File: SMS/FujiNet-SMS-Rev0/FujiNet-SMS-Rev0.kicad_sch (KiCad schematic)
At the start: 0 parts

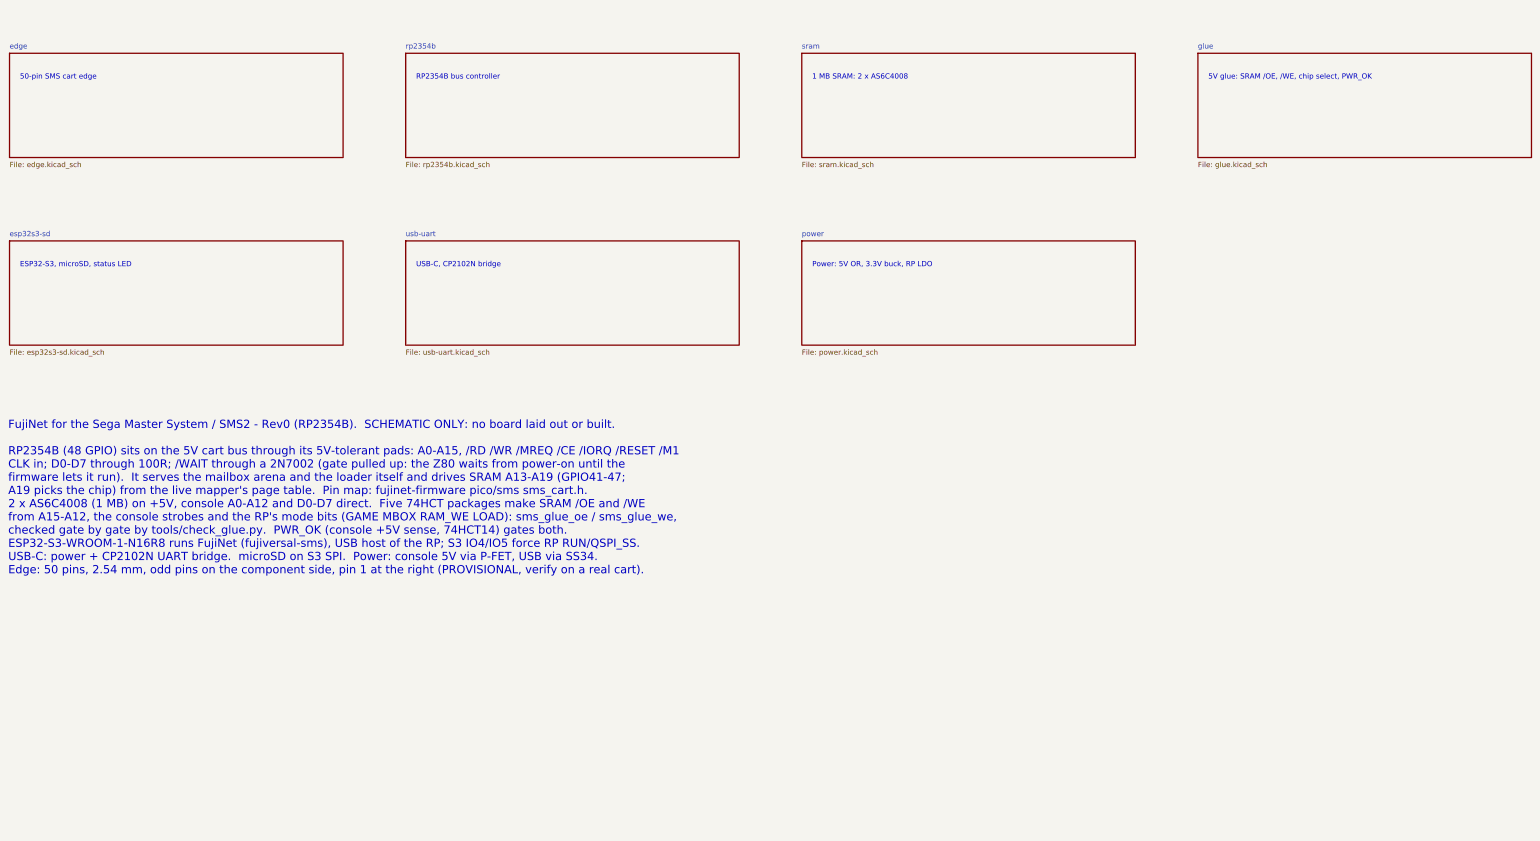
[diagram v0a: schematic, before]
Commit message: SMS Rev0: audit with kicad-happy + datasheets, fix the edge, redraw the schematic
Edge connector: every source (SMS Power slot diagram, little-scale, a 171-5519
scan, raphnet, the barbeque and reidrac footprints) puts the EVEN pins on the
component / label side with pins 1/2 at the right.  The schematic-only
footprint had the faces swapped, which would have put console +5V on /WR.
make_edge_fp.py now writes even pads on F.Cu, odd on B.Cu, 1.75 x 8.75 mm
fingers 0.75-9.5 mm from the edge on a 65.8 mm tab; check_nets.py asserts it
and tools/audit/edge_orientation.py checks it against the sources.

kicad-happy + datasheet audit (docs/design-review-rev0.md Part 1, 27 deep
review findings, gate 27/27): R_VBPD 4.7k VBUS pull-down (SS34 leakage lifts
the P-FET gate), /WAIT gate pull-up 10k -> 4.7k (GPIO34's reset pull-down vs
the 2N7002's 2.5 V threshold), 10 uF bulk on the console 5V.

Schematic: hierarchical sheets wired on a root block diagram (edge -> RP2354B
-> ESP32-S3 -> USB, glue and SRAM under the RP, power below); every sheet
drawn left to right, the glue as a wired logic network by gate depth, the
RP2354B mirrored so its bus faces the console, small sheets on A4.  Parts
are addressed by key (design.py), no more NES reference aliasing.  sch_draw
gains hierarchical labels, sheet blocks, a bus graph and flag / power-pin
lints; gen_sch checks the hierarchy against design.py and names nets by
their last path element (one bus vector per bus: KiCad joins differing
vectors by position).  ERC 0, check_nets 437/437, check_glue 8192/8192.

JLC CPL rotations measured against the EasyEDA footprint of every LCSC part
(tools/audit/jlc); the AS6C4008 has no EasyEDA footprint.

Co-Authored-By: Claude Opus 5.5 <noreply@anthropic.com>
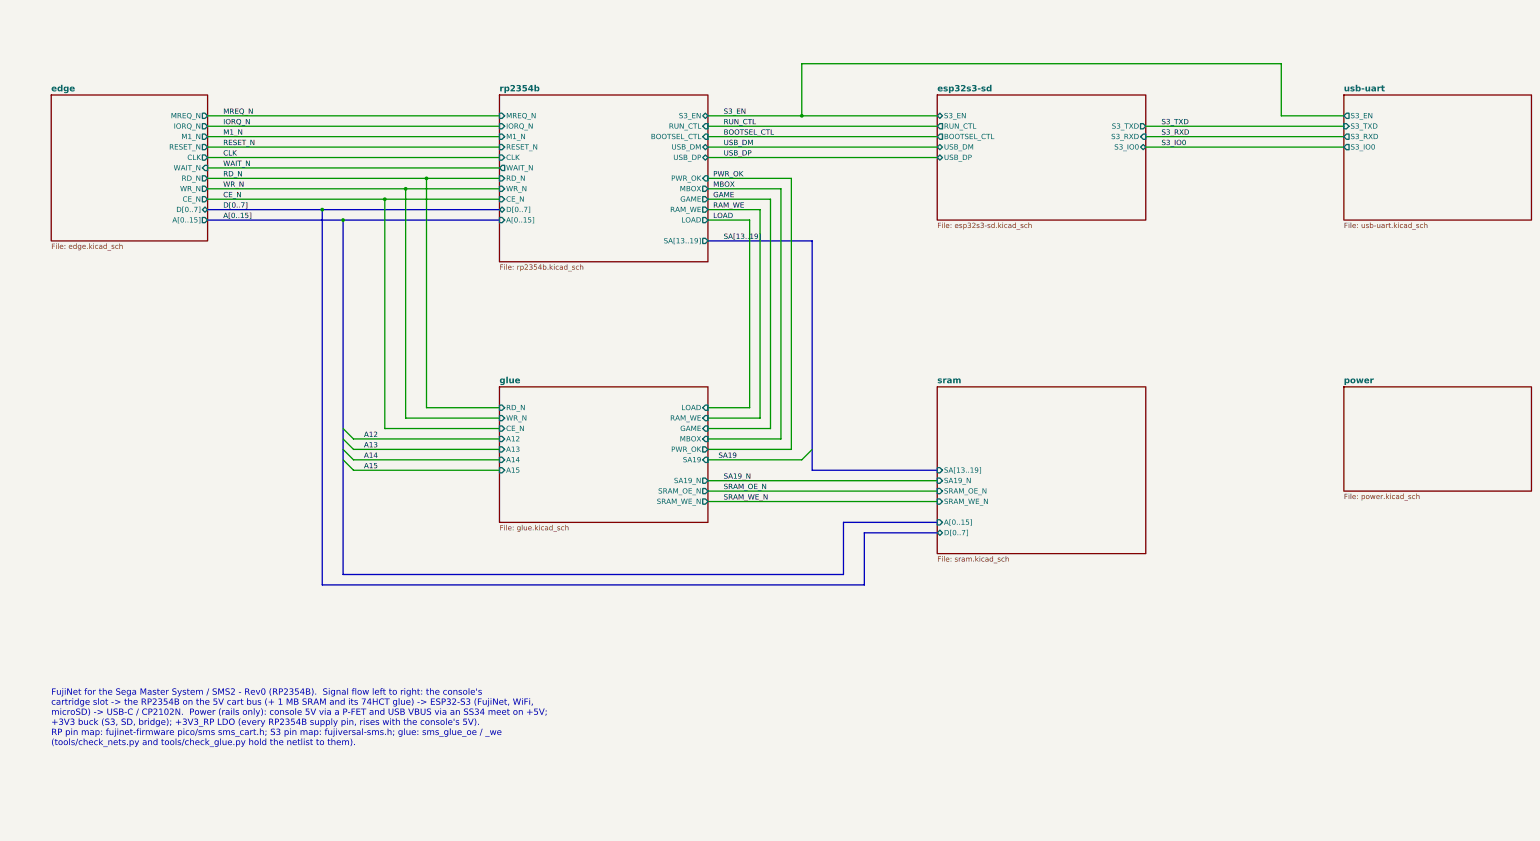
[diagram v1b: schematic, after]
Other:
- sheet edge ports: added A[0..15], CE_N, CLK, D[0..7], IORQ_N, M1_N, MREQ_N, RD_N, RESET_N, WAIT_N, WR_N; removed none
- sheet esp32s3-sd ports: added BOOTSEL_CTL, RUN_CTL, S3_EN, S3_IO0, S3_RXD, S3_TXD, USB_DM, USB_DP; removed none
- sheet glue ports: added A12, A13, A14, A15, CE_N, GAME, LOAD, MBOX, PWR_OK, RAM_WE, RD_N, SA19, SA19_N, SRAM_OE_N, SRAM_WE_N, WR_N; removed none
- sheet rp2354b ports: added A[0..15], BOOTSEL_CTL, CE_N, CLK, D[0..7], GAME, IORQ_N, LOAD, M1_N, MBOX, MREQ_N, PWR_OK, RAM_WE, RD_N, RESET_N, RUN_CTL, S3_EN, SA[13..19], USB_DM, USB_DP, WAIT_N, WR_N; removed none
- sheet sram ports: added A[0..15], D[0..7], SA19_N, SA[13..19], SRAM_OE_N, SRAM_WE_N; removed none
- sheet usb-uart ports: added S3_EN, S3_IO0, S3_RXD, S3_TXD; removed none
- note added: "FujiNet for the Sega Master System / SMS2 - Rev0 (RP2354B). Signal flow left to right: the console's cartridge slot -> the RP2354B on the 5V cart bus (+ 1 MB SRAM and its 74HCT glue) -> ESP32-S3 (FujiNet, WiFi, microSD) -> USB-C / CP2102N. Power (rails only): console 5V via a P-FET and USB VBUS via an SS34 meet on +5V; +3V3 buck (S3, SD, bridge); +3V3_RP LDO (every RP2354B supply pin, rises with 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"
- note removed: "1 MB SRAM: 2 x AS6C4008"
- note removed: "50-pin SMS cart edge"
- note removed: "5V glue: SRAM /OE, /WE, chip select, PWR_OK"
- note removed: "ESP32-S3, microSD, status LED"
- note removed: "FujiNet for the Sega Master System / SMS2 - Rev0 (RP2354B). SCHEMATIC ONLY: no board laid out or built. RP2354B (48 GPIO) sits on the 5V cart bus through its 5V-tolerant pads: A0-A15, /RD /WR /MREQ /CE /IORQ /RESET /M1 CLK in; D0-D7 through 100R; /WAIT through a 2N7002 (gate pulled up: the Z80 waits from power-on until the firmware lets it run). It serves the mailbox arena and the loader itself a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"
- note removed: "Power: 5V OR, 3.3V buck, RP LDO"
- note removed: "RP2354B bus controller"
- note removed: "USB-C, CP2102N bridge"

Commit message: SMS Rev0 v2: co-designed floorplan, region sheets, E9 pull-downs, frozen refs and nets
Floorplan study (docs/floorplan-study.md): the SMS edge is the JEDEC
32-pin memory pinout unrolled, so SRAM0 standing upright in the ROM spot
takes A0-A12 / D0-D7 / GND with no crossing.  gen_pcb.sram0_fanin draws
that fan-in locked (funnel, two corner wraps, B-finger jog vias, escape
vias for CE# and OE#).  Four candidates scored and trial-routed in
parallel; P3 (RP2354B straight north of SRAM0, SRAM1 west, glue east over
the strobes) routes best (45 unrouted after 4 passes vs 50 for the first
layout) and reads straight across on the schematic page.

- placement.py: candidates as blocks; the RP2354B + ring as a rigid macro
  (turns as a whole, dvdd_island turns with it); per-variant In4 +5V
  island polygon; label area for the shell
- design.py: sheets are board regions (cart-bus, rp-core, fujinet, usb,
  power); the RP2354B as a two-unit symbol (GPIO on cart-bus, core on
  rp-core); resistor packs one unit per resistor; RP2350-E9 4.7k
  pull-downs on GAME/LOAD/RAM_WE/MBOX/SA19 (check_nets asserts <= 8.2k);
  bring-up pads (CE, OE, WE, PWR_OK, rails, DVDD)
- geographic references (tools/annotate.py -> tools/refs.lock); net names
  frozen in tools/nets.lock (gen_sch fails if a redraw changes one)
- sch_draft.py: an every-pin-labelled draft of the final hierarchy so the
  board is built while the sheets are drawn; sch_draw lint for wired
  sheets (one piece per net, no 4-way junctions, wires clear of text,
  crossing count); sch_place.py mirror check
- check_parts_inside: footprint keep-outs (the S3 antenna bars parts)
- shell: RESET plunger redesigned (captive flange under the guide, stem
  on the TS-1187A actuator, travel asserts, interference part)

ERC 0, parity 126/126, check_nets 442/442, check_glue 8192/8192.
Board placed, not routed yet.

Co-Authored-By: Claude Opus 5.5 <noreply@anthropic.com>
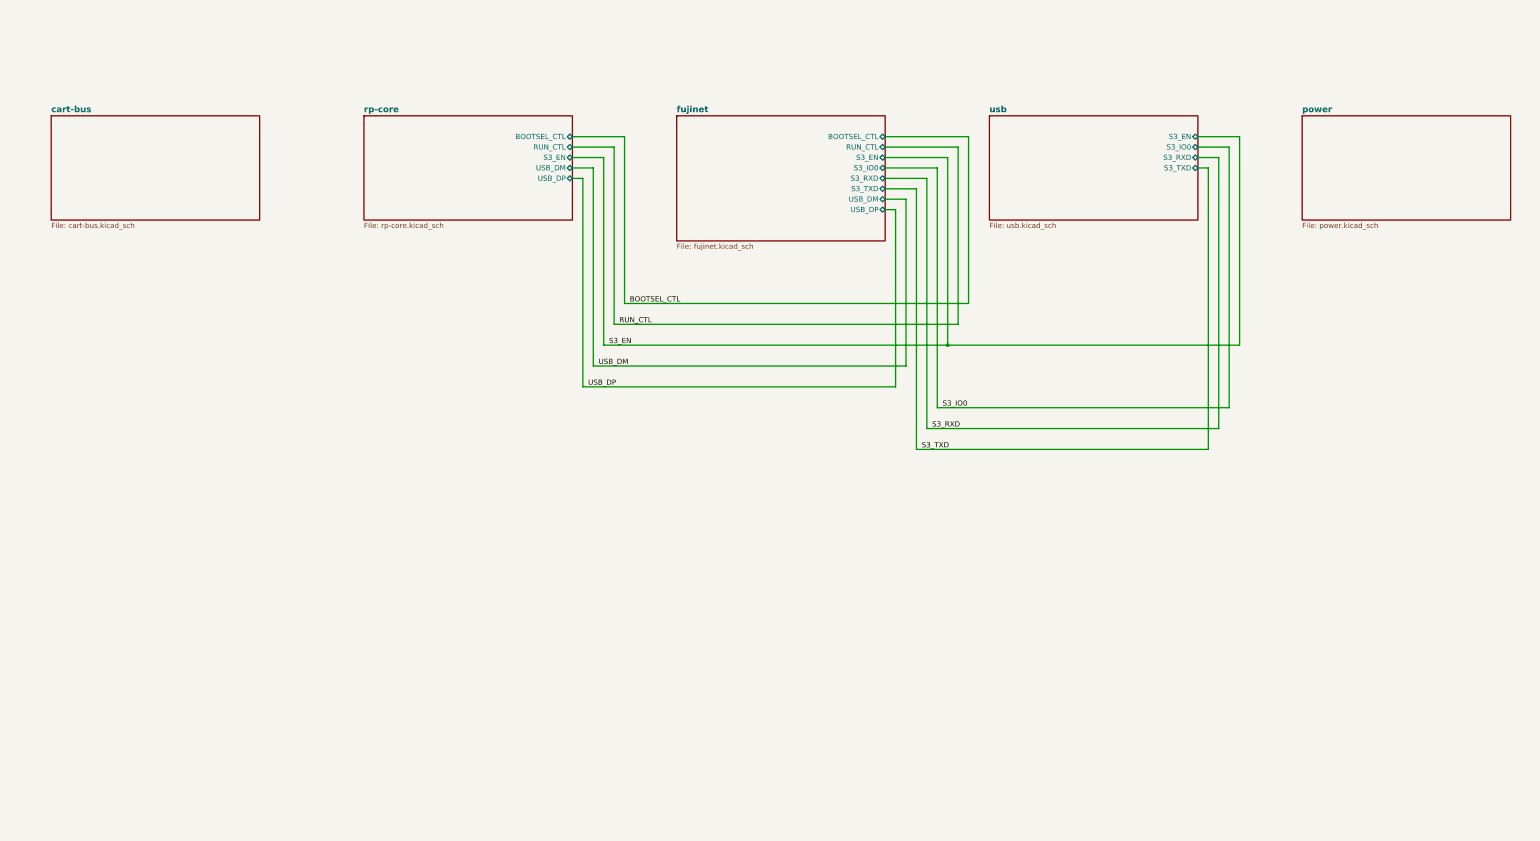
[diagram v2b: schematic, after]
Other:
- removed sheet edge
- removed sheet esp32s3-sd
- removed sheet glue
- removed sheet rp2354b
- removed sheet sram
- removed sheet usb-uart
- added sheet cart-bus (cart-bus.kicad_sch)
- added sheet fujinet (fujinet.kicad_sch)
- added sheet rp-core (rp-core.kicad_sch)
- added sheet usb (usb.kicad_sch)
- note removed: "FujiNet for the Sega Master System / SMS2 - Rev0 (RP2354B). Signal flow left to right: the console's cartridge slot -> the RP2354B on the 5V cart bus (+ 1 MB SRAM and its 74HCT glue) -> ESP32-S3 (FujiNet, WiFi, microSD) -> USB-C / CP2102N. Power (rails only): console 5V via a P-FET and USB VBUS via an SS34 meet on +5V; +3V3 buck (S3, SD, bridge); +3V3_RP LDO (every RP2354B supply pin, rises with 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"

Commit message: SMS Rev0 v2: redraw every sheet to mirror the board
Each sheet is now hand-placed in tools/sch_layout.py from where its parts
sit on the board, turned so the edge fingers face left (south -> left,
north -> right, west -> top, east -> bottom), and every connection on a
sheet is a wire:

- rp-core: the RP2354B core unit with its decoupling ring at the pins, the
  regulator corner, the crystal, SWD, RUN / BOOTSEL and the RESET diode
  (planar).
- fujinet: a functional ESP32-S3 symbol, EN / BOOT, the WS2812, and the
  microSD's SPI lines stepping into the socket with the pull-ups between
  them (planar).
- usb: a functional USB-C symbol, the CP2102N mirrored to face the
  receptacle, and the auto-program pair.  This page has one crossing, which
  cannot be avoided: RTS and DTR sit side by side on the bridge and each
  feeds the base of one transistor and the emitter of the other.
- power: the CONS_5V / VBUS OR on one +5V line, the LDO above it, the buck
  below it, and the rail PWR_FLAGs grouped together (planar).
- root: the board outline at 2:1, turned the same way, with each sheet's
  block at its region and the nine signals between sheets wired without a
  crossing; notes cover the stack-up and the firmware contract.

Gates: gen_sch.py checks the mirror (Kendall tau >= 0.85 per axis for the
major parts, multi-unit packages counted at the centre of their units,
parts within 5 mm on the board counted as level; every sheet is at
1.00 / 1.00) and a crossing budget per sheet (cart-bus 75, usb 1,
others 0).  ERC is 0 at all severities, netlist parity holds, the net
names equal tools/nets.lock, check_nets passes 442/442, check_glue
8192/8192, and edge_orientation passes.

Co-Authored-By: Claude Opus 5.5 <noreply@anthropic.com>
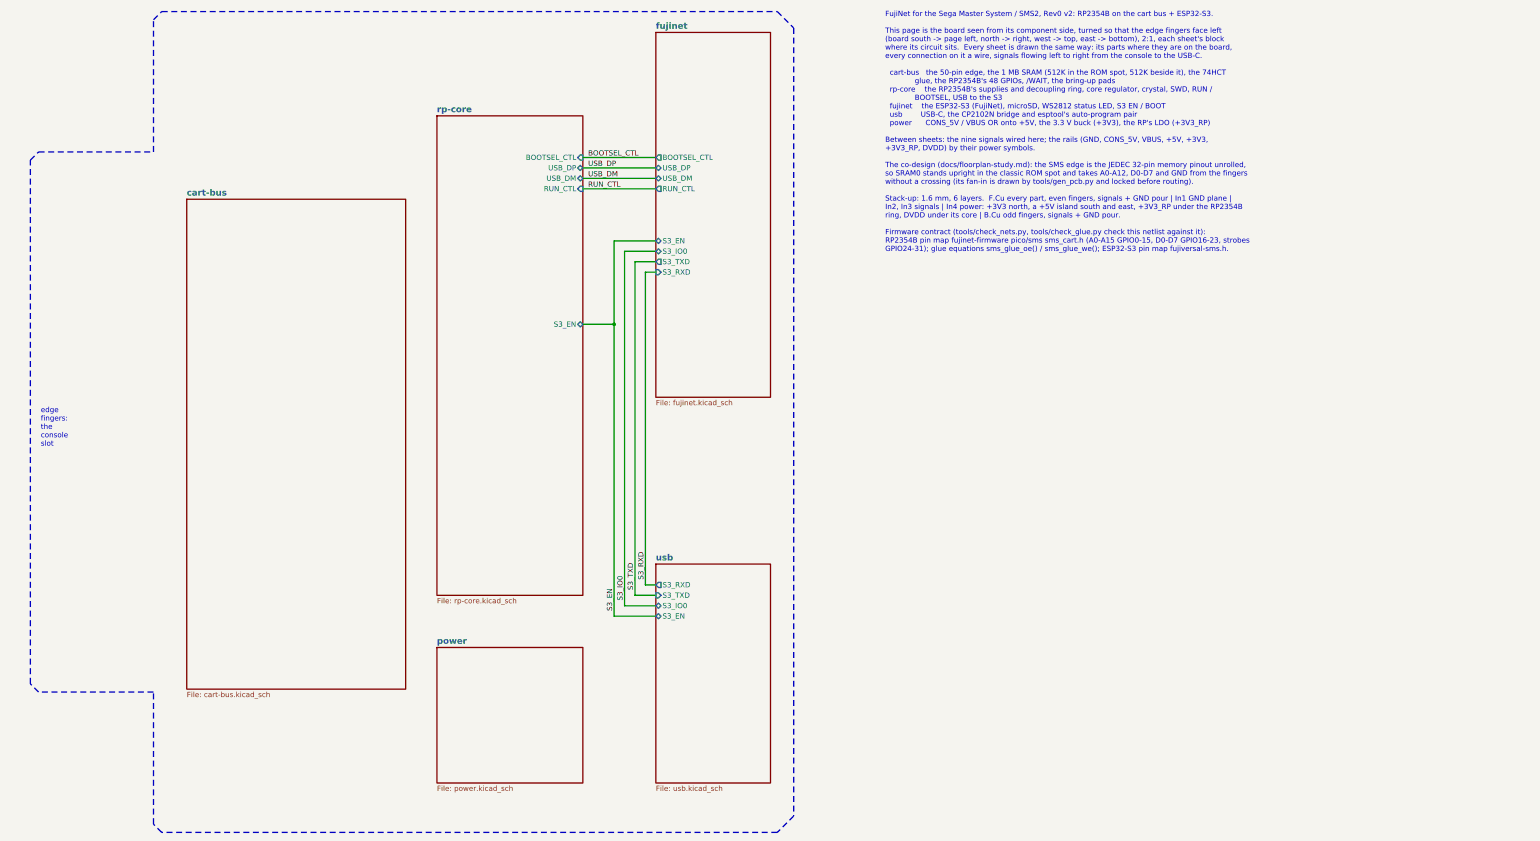
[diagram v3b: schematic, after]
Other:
- note added: "FujiNet for the Sega Master System / SMS2, Rev0 v2: RP2354B on the cart bus + ESP32-S3. This page is the board seen from its component side, turned so that the edge fingers face left (board south -> page left, north -> right, west -> top, east -> bottom), 2:1, each sheet's block where its circuit sits. Every sheet is drawn the same way: its parts where they are on the board, every connection on i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"
- note added: "edge fingers: the console slot"
